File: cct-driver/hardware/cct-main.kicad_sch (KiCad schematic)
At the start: 195 parts, among them J1 C707824, J10 C37815, J11 C474923, J2 C165948, J3 C441333, J4 C441333, J5 C441333, J6 C441333, J7 C441333, J8 C441333, J9 C2906270, Q1 C3281500, Q10 C2890395, Q11 C2890395, Q12 C2890395, Q13 C2890395, Q14 C2890395, Q15 C2890395, Q16 C2890395, Q17 C2890395, Q18 C2890395, Q2 C3281500, Q3 C20526, Q4 C2146, Q5 C2146, Q6 C20526, Q7 C2890395, Q8 C2890395, Q9 C2890395, SW1 C318884, SW2 C318884, U1 C2864837, U2 C524806, U3 C6186, U4 C701341, U5 C84681, U6 C52140501, U7 C52140501

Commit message: 料号回到一个源头:板文件 Value 与原理图都跟上 gen_sch.py
摸清了「重生成原理图会让 parity 从 205 涨到 209」的真正原因 —— **不是生成器写错了,
是板文件那份 Value 落后了六天。**

本工程料号只有一个源头:`gen_sch.py` 的 part() 表,`gen_bom.py` 直接解析它出 BOM。
但板文件里每个封装还各自带一份 Value(F.Fab 层文字),**没有任何一步会去更新它**。
2026-08-07 把 6 个精密电阻 + 1 个 C0G 电容换成真实料号时只改了 gen_sch.py,于是:

    R62 C25804→C25811   R63 C25803→C402870  R64 C25804→C22892   R65 C23162→C25972
    R66 C25803→C23208   R67 C25804→C12447   C40 C14663→C107035

BOM 一直是对的(它读 gen_sch.py),错的是板文件和原理图。重新生成原理图时
KiCad 就会逐个报 `Value (R62) doesn't match symbol value`,正好 7 条 —— 这就是
那 +4 的来源(7 条新增、3 条消失)。

新增 `gen_sync_values.py` 把板文件 Value 同步回 gen_sch.py(幂等,带 --check
模式),同步了这 7 处,然后重新生成原理图。

验收:
- schematic-parity **205 → 205**,与基线完全一致(不再有 Value 不匹配那 7 条)
- DRC **76**,0 未连接
- **出货 Gerber 九层逐字节相同**(与同步前的 HEAD 比):Value 在 F.Fab 层,
  不进任何出货文件;`cpl-jlc.csv` 不含 Value 列;`bom-jlc.csv` 读的是 gen_sch.py。
  唯一会变的是 `pos-raw.csv` 的 Val 列(KiCad 原始导出,仅供人看)

README 加了一节「料号只有一个源头」,写清改完料号要跑哪两条,并记下这次的教训:
**gen_sch.py 能不能跑通本身就是个健康检查** —— 它坏了六天没人发现,
是因为没有任何一步会去碰它。

Co-Authored-By: Claude <noreply@anthropic.com>
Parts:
- removed R63, R66: C25803, symbol cct:0603WAF1003T5E
- removed R65: C23162, symbol cct:0603WAF4701T5E
- added R63: C402870, symbol cct:0603WAF1002T5E
- added R65: C25972, symbol cct:0603WAF1002T5E
- added R66: C23208, symbol cct:0603WAF1002T5E
- C40: value C14663 -> C107035
- R62: value C25804 -> C25811
- R64: value C25804 -> C22892
- R67: value C25804 -> C12447
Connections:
- net COMP: now also R65.1
- net COMP_Z: now also R65.2
- net EN_BUCK: now also R66.2
- net FB_5V: now also R63.2
- net V24_LOGIC: now also R66.1
- net V5_BUCK: now also R63.1
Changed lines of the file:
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@@
     (in_bom yes) (on_board yes)
     (property "Reference" "R62" (at 120.65 68.12 0) (effects (font (size 1.27 1.27))))
-    (property "Value" "C25804" (at 120.65 74.12 0) (effects (font (size 1.27 1.27))))
+    (property "Value" "C25811" (at 120.65 74.12 0) (effects (font (size 1.27 1.27))))
     (pin "2")
     (pin "1")
@@
   (global_label "RT_CLK" (shape passive) (at 115.57000000000001 71.12 180) (effects (font (size 1.27 1.27)) (justify left)))
   (global_label "GND" (shape passive) (at 125.73 71.12 0) (effects (font (size 1.27 1.27)) (justify left)))
-  (symbol (lib_id "cct:0603WAF1003T5E") (at 120.65 86.36 0) (unit 1)
+  (symbol (lib_id "cct:0603WAF1002T5E") (at 120.65 86.36 0) (unit 1)
     (in_bom yes) (on_board yes)
     (property "Reference" "R63" (at 120.65 83.36 0) (effects (font (size 1.27 1.27))))
-    (property "Value" "C25803" (at 120.65 89.36 0) (effects (font (size 1.27 1.27))))
+    (property "Value" "C402870" (at 120.65 89.36 0) (effects (font (size 1.27 1.27))))
     (pin "2")
     (pin "1")
@@
     (in_bom yes) (on_board yes)
     (property "Reference" "R64" (at 120.65 98.6 0) (effects (font (size 1.27 1.27))))
-    (property "Value" "C25804" (at 120.65 104.6 0) (effects (font (size 1.27 1.27))))
+    (property "Value" "C22892" (at 120.65 104.6 0) (effects (font (size 1.27 1.27))))
     (pin "2")
     (pin "1")
@@
   (global_label "FB_5V" (shape passive) (at 115.57000000000001 101.6 180) (effects (font (size 1.27 1.27)) (justify left)))
   (global_label "GND" (shape passive) (at 125.73 101.6 0) (effects (font (size 1.27 1.27)) (justify left)))
-  (symbol (lib_id "cct:0603WAF4701T5E") (at 120.65 116.84 0) (unit 1)
+  (symbol (lib_id "cct:0603WAF1002T5E") (at 120.65 116.84 0) (unit 1)
     (in_bom yes) (on_board yes)
     (property "Reference" "R65" (at 120.65 113.84 0) (effects (font (size 1.27 1.27))))
-    (property "Value" "C23162" (at 120.65 119.84 0) (effects (font (size 1.27 1.27))))
+    (property "Value" "C25972" (at 120.65 119.84 0) (effects (font (size 1.27 1.27))))
     (pin "2")
     (pin "1")
@@
     (in_bom yes) (on_board yes)
     (property "Reference" "C40" (at 120.65 144.32 0) (effects (font (size 1.27 1.27))))
-    (property "Value" "C14663" (at 120.65 150.32 0) (effects (font (size 1.27 1.27))))
+    (property "Value" "C107035" (at 120.65 150.32 0) (effects (font (size 1.27 1.27))))
     (pin "1")
     (pin "2")
@@
   (global_label "COMP" (shape passive) (at 115.57000000000001 147.32 180) (effects (font (size 1.27 1.27)) (justify left)))
   (global_label "GND" (shape passive) (at 125.73 147.32 0) (effects (font (size 1.27 1.27)) (justify left)))
-  (symbol (lib_id "cct:0603WAF1003T5E") (at 120.65 162.56 0) (unit 1)
+  (symbol (lib_id "cct:0603WAF1002T5E") (at 120.65 162.56 0) (unit 1)
     (in_bom yes) (on_board yes)
     (property "Reference" "R66" (at 120.65 159.56 0) (effects (font (size 1.27 1.27))))
-    (property "Value" "C25803" (at 120.65 165.56 0) (effects (font (size 1.27 1.27))))
+    (property "Value" "C23208" (at 120.65 165.56 0) (effects (font (size 1.27 1.27))))
     (pin "2")
     (pin "1")
@@
     (in_bom yes) (on_board yes)
     (property "Reference" "R67" (at 120.65 174.8 0) (effects (font (size 1.27 1.27))))
-    (property "Value" "C25804" (at 120.65 180.8 0) (effects (font (size 1.27 1.27))))
+    (property "Value" "C12447" (at 120.65 180.8 0) (effects (font (size 1.27 1.27))))
     (pin "2")
     (pin "1")

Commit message: 指示灯改到输出端取信号,并挪到保险丝与端子之间
12 颗通道指示灯原来接在 74HCT245 输出侧(栅阻之前)、阴极经 4.7k 到 GND,位置
由 gen_pcb.py 里一串手写的 x 槽位决定,跟通道列毫无关系 —— 这就是"灯排得对不上
是哪一路"的根因(CH5 那一对甚至被劈开 45mm)。

改成跨在本路输出端子的 V+ 与漏极之间,与灯带并联:

    CHn_VOUT ──▶| LEDn ──[ 40.2k ]── CHn_CW_D / CHn_WW_D ──▶ MOS 漏极

**最大的收获不是好看,是 V+ 取自支路保险丝下游** —— V24_BUS 与 CHn_VOUT 之间
只隔着 F2–F7 一个器件,所以**支路丝一断,那一路的灯直接灭**。下单清单里一直记着
「支路丝断 = 逻辑全正常、只有输出不通 = 最容易被误判成坏板」,现在板子自己会说。

与灯带并联不是串联:不接灯带照常亮,灯带也不会有残光。限流 40.2k(C12447,
R67 已在用,不新增料号)给 0.53mA,与原来 5V+4.7k 的 0.51mA 亮度基本一致;
0603 上压降 21.4V、功耗 11mW(额定 100mW),28V 时 0.63mA / 16mW。

摆位:保险丝与端子之间那条带。**这条带看着有 5.06mm,实际可用只有 1.46mm** ——
上沿被每路 2 个 Ø1.0 的 V24_BUS 缝合过孔(y=129.04)吃掉,下沿(CH1)被 TP6 的
courtyard 吃掉。解法不是搬 TP6,而是把它那个对 1.5mm 焊盘明显偏大的 courtyard
收到 IPC 尺寸(2.59→2.0,纯 DRC 构造,不动铜不动实物,**TP6 坐标一个字没改**),
上沿退到 131.46,四个件整排落在它上方,行位 y=130.55。
CH6 单独右移 0.55mm:它的 V+ 主铜在 y<130 处斜着往右拐,那条斜线的边缘实测离
常规位置的阴极盘只差 0.004mm。

丝印:这条带塞不下 4 个位号,而人要读的是"哪一路的冷白还是暖白"(通道号板子
下缘本来就印着)。所以这 24 个件的位号隐藏(装配用坐标文件;位号在 cpl/BOM/
原理图里都在),改成每颗灯旁边印 CW / WW;端子引脚的 V+/CW/WW 挪到端子下方,
更贴近接线那一头;F2–F7 与 J3–J8 的位号挪到各自的列间空隙。

验收(全部踩在基线上或更好):
- DRC **72**(基线 76),**0 未连接**;clearance 4(J2 老账)、silk_edge 10、
  silk_over_copper 53 全部持平,silk_overlap **5**(基线 9,反而更干净)
- schematic-parity **205**,与基线一模一样
- **网表 diff 只有该动的 31 个网络**:12 个 LED 阳极 CH*_x_G→CH*_VOUT、
  12 个电阻另一端 GND→CH*_x_D、GND 少这 12 个焊盘。其余一条没动
- 六路主电流路径复量仍是 **2.0mm**
- 丝印渲染图看过:每路两颗灯正对自己的端子,灯下方印 CW/WW,端子下方 V+/CW/WW
  与 CH1–CH6,一眼对得上

拆成三个脚本是被 pcbnew 的两个坑逼的,都在脚本里留了路标:
① `GraphicalItems()` 在动过封装位置之后不能再迭代 → 电阻外框改走文本层
   (gen_strip_res_silk.py,幂等 + --check,只动那 12 个,灯的外框与极性标记不碰);
② 大量 board.Remove() 之后连 GetFootprints() 都会失效,**存盘重读也救不回来**
   → 丝印拆成独立进程(gen_led_silk.py)。

顺带修好 gen_sync_values.py:它原来用正则抠 part("R62","C25811",...),而 6 个通道
是在循环里写的 `part(Rlc, "C12447", ...)` —— **位号是变量,正则抠不到**,那 12 个
电阻的料号一直同步不到板上。改成直接执行 gen_sch.py 的元件表。

Co-Authored-By: Claude <noreply@anthropic.com>
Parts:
- removed R20, R21, R26, R27, R32, R33, R38, R39, R44, R45, R50, R51: C23162, symbol cct:0603WAF4701T5E
- added R20, R21, R26, R27, R32, R33, R38, R39, R44, R45, R50, R51: C12447, symbol cct:0603WAF1002T5E
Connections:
- net CH1_CW_D: now also R20.2
- net CH1_CW_G: no longer LED2.1 (A)
- net CH1_VOUT: now also LED2.1 (A), LED3.1 (A)
- net CH1_WW_D: now also R21.2
- net CH1_WW_G: no longer LED3.1 (A)
- net CH2_CW_D: now also R26.2
- net CH2_CW_G: no longer LED4.1 (A)
- net CH2_VOUT: now also LED4.1 (A), LED5.1 (A)
- net CH2_WW_D: now also R27.2
- net CH2_WW_G: no longer LED5.1 (A)
- net CH3_CW_D: now also R32.2
- net CH3_CW_G: no longer LED6.1 (A)
- net CH3_VOUT: now also LED6.1 (A), LED7.1 (A)
- net CH3_WW_D: now also R33.2
- net CH3_WW_G: no longer LED7.1 (A)
- net CH4_CW_D: now also R38.2
- net CH4_CW_G: no longer LED8.1 (A)
- net CH4_VOUT: now also LED8.1 (A), LED9.1 (A)
- net CH4_WW_D: now also R39.2
- net CH4_WW_G: no longer LED9.1 (A)
- net CH5_CW_D: now also R44.2
- net CH5_CW_G: no longer LED10.1 (A)
- net CH5_VOUT: now also LED10.1 (A), LED11.1 (A)
- net CH5_WW_D: now also R45.2
- net CH5_WW_G: no longer LED11.1 (A)
- net CH6_CW_D: now also R50.2
- net CH6_CW_G: no longer LED12.1 (A)
- net CH6_VOUT: now also LED12.1 (A), LED13.1 (A)
- net CH6_WW_D: now also R51.2
- net CH6_WW_G: no longer LED13.1 (A)
- net LED10_K: now also R44.1
- net LED11_K: now also R45.1
- net LED12_K: now also R50.1
- net LED13_K: now also R51.1
- net LED2_K: now also R20.1
- net LED3_K: now also R21.1
- net LED4_K: now also R26.1
- net LED5_K: now also R27.1
- net LED6_K: now also R32.1
- net LED7_K: now also R33.1
- net LED8_K: now also R38.1
- net LED9_K: now also R39.1

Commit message: v2 输入级:Q1/Q2 改成真防反接,总断路从 24V 母线挪到 /OE
三件事,都在 Block A,零新增有源器件。

1) Q1/Q2 的 D 与 S 对调,DZ1 阴极跟着从 V24_FUSED 改到 V24_PROT。
   P 沟道体二极管是漏(阳)→源(阴),要防反接就得让它顺着正常负载电流方向,
   也就是漏极接进线侧。改完:反接时体二极管反偏、|Vds|=24V(手册 −60V)、
   Vgs=0V,整条路径零电流零损坏。DZ1 必须跟着走,留在 V24_FUSED 的话反接时
   它会正偏把栅极拉到 −23V,MOS 反而全开。

   代价写在文档里:防反接接法下体二极管在栅极动之前就把浪涌放过去了,
   所以"栅极缓启动"在这个接法下做不了,也不该做。顺带把"栅-源加电容能控
   dV/dt"这条也否掉了 —— 米勒平台期间 Vgs 恒定,栅-源电容电流为零,
   要控 dV/dt 电容得加在栅-漏之间。

2) 总断路开关从 24V 母线挪到 /OE。留在母线上会切掉 ESP32 自己的供电
   (PTC1 从 Q1/Q2 下游取电),变成约 1Hz 的张弛振荡器。
   Q3 集电极 PMOS_GATE → OE_B,R2 从 MASTER_OFF_B→GND 改成 TP7→基极。
   Q3 导通把 OE_B 钳到 0.1V,压过固件让 12 路输出全高阻。
   控制端引到 TP7 焊盘,不占 GPIO(26 个可用脚已全部分配,文档里逐个数过)。
   默认下拉、悬空即安全;误接 GND 是正常工作,误接 24V 只是全灭不会坏。
   给了完整的 MASTER_OFF 状态表。

3) 进线阻尼 RC(C44 4.7µF/100V + R68 1Ω)与母线陶瓷 C45/C46,
   都用已在用的料号 C381466,不新增电容料号。挂在 F1 下游而不是 V24_IN:
   1210 陶瓷开裂典型是短路,挂 V24_IN 上保险丝管不了它。
   R68=1Ω 是起始值不是算出来的,定值方法与实测步骤写进文档。
   顺带纠正:42.1V 是 SMBJ26A 的钳位天花板,不是实测到的振铃。

另:RS1 换掉停产的 C500614 → C459679(2mΩ ±1% 3W 合金,TCR ±50ppm/℃,
与原件上界持平,固件 shunt_resistance 不用改);R63 的 C402870 库存只剩
1977,换同值大库存的 C22858。全部 47 个料号供货复查结果记进 §A2.7。

元件 195 → 199(+C44/C45/C46/R68),含测试点安装孔 205 → 212(+TP7/TP8/TP9)。
四处清单一致性已用 check-partlist-consistency.py 核过,全绿。
ERC:0 错误,警告 1 → 2(新增的那条是 MASTER_OFF_TP 只连一个引脚,预期行为)。

PCB / gerber / CPL 一个字节没动 —— order-checklist.md 顶部已加下单禁令。

Co-Authored-By: Claude <noreply@anthropic.com>
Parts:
- added C44, C45, C46: C381466, symbol cct:FS32X475K101EGG
- added R68: C17928, symbol cct:0603WAF1002T5E
- R63: value C402870 -> C22858
- RS1: value C500614 -> C459679
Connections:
- net GND: now also C45.2, C46.2, R68.2; no longer R2.2
- net MASTER_OFF_B: now also R2.2; no longer R2.1
- net OE_B: now also Q3.3 (C)
- net PMOS_GATE: no longer Q3.3 (C)
- net V24_BUS: now also C46.1
- net V24_FUSED: now also Q1.2 (D), Q2.2 (D), C44.1; no longer DZ1.1 (K), Q1.3 (S), Q2.3 (S)
- net V24_PROT: now also DZ1.1 (K), Q1.3 (S), Q2.3 (S), C45.1; no longer Q1.2 (D), Q2.2 (D)
- new net MASTER_OFF_TP: R2.1
- new net SNUB_MID: C44.2, R68.1

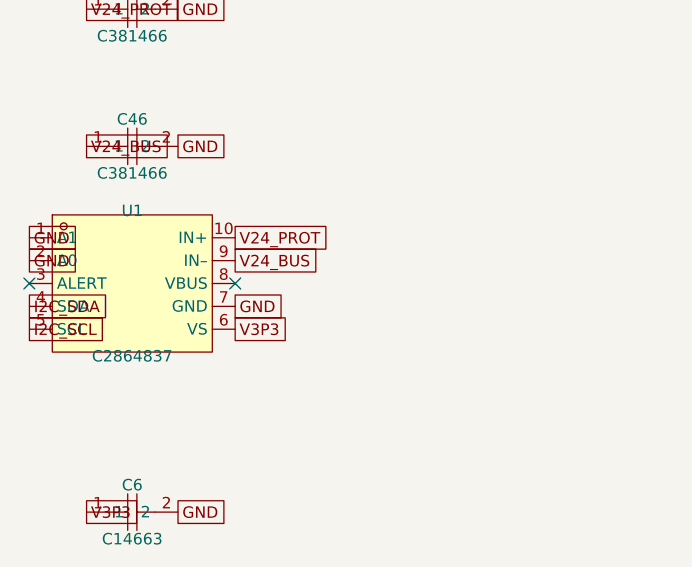
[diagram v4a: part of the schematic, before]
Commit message: fix(schematic): connect INA237 VBUS to load bus
Co-Authored-By: Claude <noreply@anthropic.com>
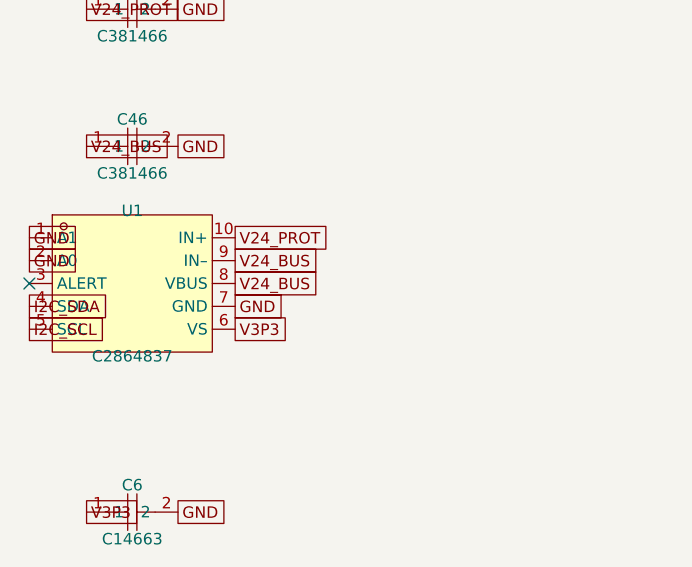
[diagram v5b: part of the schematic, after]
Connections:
- net V24_BUS: now also U1.8 (VBUS)
- no-connect marks 31 -> 30
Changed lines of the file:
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@@
   (global_label "GND" (shape passive) (at 19.05 368.3 180) (effects (font (size 1.27 1.27)) (justify left)))
   (global_label "GND" (shape passive) (at 19.05 365.76000000000005 180) (effects (font (size 1.27 1.27)) (justify left)))
+  (global_label "V24_BUS" (shape passive) (at 41.91 370.84000000000003 0) (effects (font (size 1.27 1.27)) (justify left)))
   (no_connect (at 19.05 370.84000000000003))
-  (no_connect (at 41.91 370.84000000000003))
   (symbol (lib_id "cct:CC0603KRX7R9BB104") (at 30.48 396.24 0) (unit 1)
     (in_bom yes) (on_board yes)

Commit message: 原理图修两条 🔴：下载电路的发射极交叉接回去，OE 下拉换成 4.7k
🔴-1 Q4.E / Q5.E 从 GND 改接对方那根控制线：
  Q4:B=RTS_B(来自 DTR#) / E=RTS / C=EN
  Q5:B=DTR_B(来自 RTS#) / E=DTR / C=IO0
Espressif 参考电路要的是异或型行为——DTR#/RTS# 同电平时两管都截止，
板子正常运行；只有一高一低才动 EN 或 IO0。这个性质靠的就是「基极接一根、
发射极接另一根」。原来两个发射极都接 GND，它退化成两个普通反相器，而
CH340C 的 DTR#/RTS# 是低有效输出、空闲都是高，于是 EN 被钉低、IO0 也被
钉低：esptool 时序第三拍会把芯片按回复位并一直按着，串口一关板子就停机。

修完的真值表（DTR#/RTS# 是芯片脚电平）：
  高/高 → EN 高、IO0 高（正常运行，串口空闲就是这个状态）
  低/低 → EN 高、IO0 高（正常运行）
  高/低 → EN 低（复位）
  低/高 → IO0 低（进下载模式）
基极电流 (3.3−0.7)/10k = 260µA，拉低 EN 只需吸 330µA → 需要的 β 是 1.3。

🔴-2 R15 100k → 4.7k（C23162，R52/R53 已在用，不新增料号）：
GPIO15 = MTDO 带 45kΩ 内部上拉（ESP32 手册 Table 3-1 和 Table IO_MUX 的
At Reset / After Reset 都是 wpu），经 R14 灌 40µA 进 Q6 基极就足够让它饱和，
于是两片 245 在整个启动期间是使能的。4.7k 在 0.7V 时要吸 149µA，大于内部
上拉能给的 75µA → Q6 铁定截止；而固件把 GPIO15 驱动到 3.3V 时基极还有
111µA，×hFE 40 = 4.4mA，远大于需要的 0.5mA。

🟡-1 C12 10µF → 1µF/50V X7R 0805（C28323，基础库，同封装）：
10µF 时 R4·C12 = 100ms，EN 要 138ms 才过 VIH(2.475V)，而 esptool 释放 EN
之后只等 50ms 就放掉 IO0。1µF 时 13.8ms 过 VIH，上电复位延时仍然够。
这条和 🔴-1 是一件事，不改它时序照样对不上。

ERC：0 错误 / 2 警告（MASTER_OFF_TP 的 isolated_pin_label 与 L1 的
lib_symbol_mismatch，两条都是既有的、netlist-spec §A2.3 里写过）。
导出网表实测：DTR = {U5.13, R11.1, Q5.E}、RTS = {U5.14, R12.1, Q4.E}。

Co-Authored-By: Claude <noreply@anthropic.com>
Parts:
- removed R15: C25803, symbol cct:0603WAF1003T5E
- added R15: C23162, symbol cct:0603WAF4701T5E
- C12: value C15850 -> C28323
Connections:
- net DTR: now also Q5.2 (E)
- net GND: now also R15.2; no longer Q4.2 (E), Q5.2 (E)
- net OE_B: now also R15.1
- net RTS: now also Q4.2 (E)
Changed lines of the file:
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@@
     (in_bom yes) (on_board yes)
     (property "Reference" "C12" (at 120.65 456.74 0) (effects (font (size 1.27 1.27))))
-    (property "Value" "C15850" (at 120.65 462.74 0) (effects (font (size 1.27 1.27))))
+    (property "Value" "C28323" (at 120.65 462.74 0) (effects (font (size 1.27 1.27))))
     (pin "2")
     (pin "1")
@@
   (global_label "RTS_B" (shape passive) (at 208.28 205.74 180) (effects (font (size 1.27 1.27)) (justify left)))
   (global_label "EN" (shape passive) (at 213.35999999999999 200.66 90) (effects (font (size 1.27 1.27)) (justify left)))
-  (global_label "GND" (shape passive) (at 213.35999999999999 210.82000000000002 270) (effects (font (size 1.27 1.27)) (justify left)))
+  (global_label "RTS" (shape passive) (at 213.35999999999999 210.82000000000002 270) (effects (font (size 1.27 1.27)) (justify left)))
   (symbol (lib_id "cct:S8050_C2146") (at 210.82 231.14 0) (unit 1)
     (in_bom yes) (on_board yes)
@@
   (global_label "DTR_B" (shape passive) (at 208.28 231.14000000000001 180) (effects (font (size 1.27 1.27)) (justify left)))
   (global_label "IO0" (shape passive) (at 213.35999999999999 226.06 90) (effects (font (size 1.27 1.27)) (justify left)))
-  (global_label "GND" (shape passive) (at 213.35999999999999 236.22000000000003 270) (effects (font (size 1.27 1.27)) (justify left)))
+  (global_label "DTR" (shape passive) (at 213.35999999999999 236.22000000000003 270) (effects (font (size 1.27 1.27)) (justify left)))
   (symbol (lib_id "cct:0603WAF1002T5E") (at 210.82 256.54 0) (unit 1)
     (in_bom yes) (on_board yes)
@@
   (global_label "OE_CTRL" (shape passive) (at 205.73999999999998 434.34000000000003 180) (effects (font (size 1.27 1.27)) (justify left)))
   (global_label "OE_B" (shape passive) (at 215.9 434.34000000000003 0) (effects (font (size 1.27 1.27)) (justify left)))
-  (symbol (lib_id "cct:0603WAF1003T5E") (at 210.82 449.58 0) (unit 1)
+  (symbol (lib_id "cct:0603WAF4701T5E") (at 210.82 449.58 0) (unit 1)
     (in_bom yes) (on_board yes)
     (property "Reference" "R15" (at 210.82 446.58 0) (effects (font (size 1.27 1.27))))
-    (property "Value" "C25803" (at 210.82 452.58 0) (effects (font (size 1.27 1.27))))
-    (pin "2")
-    (pin "1")
+    (property "Value" "C23162" (at 210.82 452.58 0) (effects (font (size 1.27 1.27))))
+    (pin "2")
+    (pin "1")
